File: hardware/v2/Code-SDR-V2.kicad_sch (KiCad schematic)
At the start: 0 parts

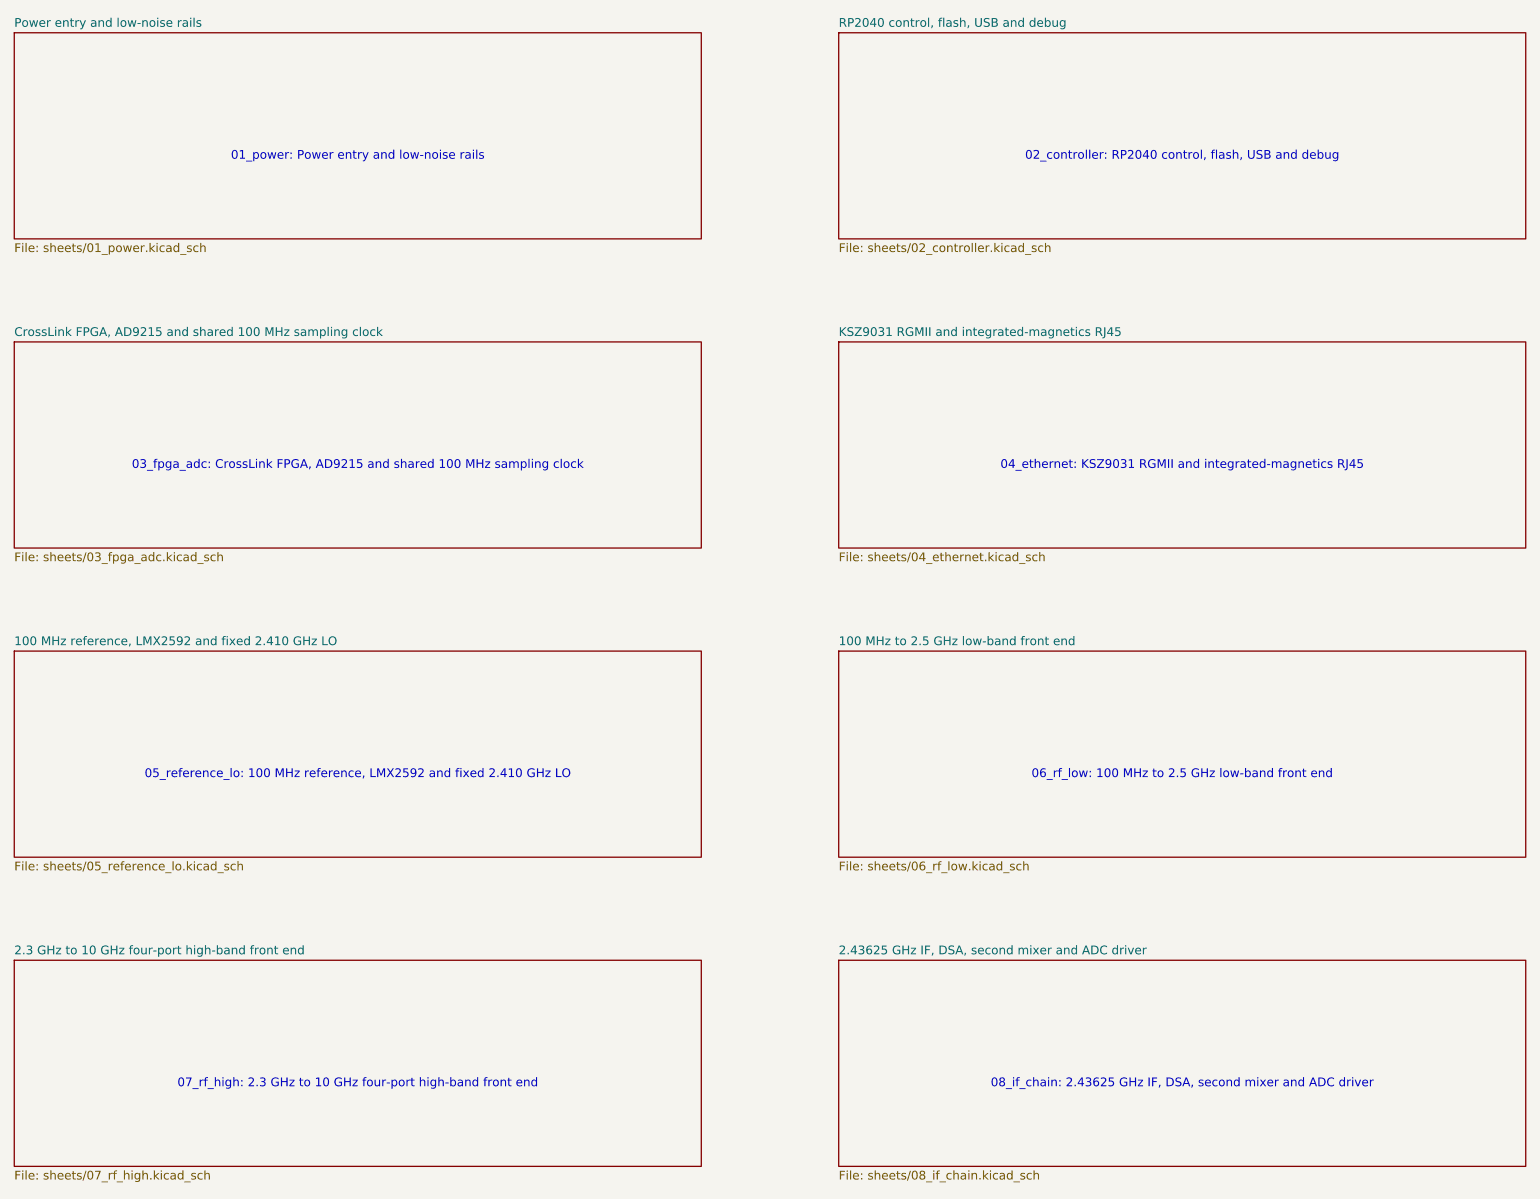
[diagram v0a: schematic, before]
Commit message: hardware: checkpoint corrected V2 routing at 108 opens
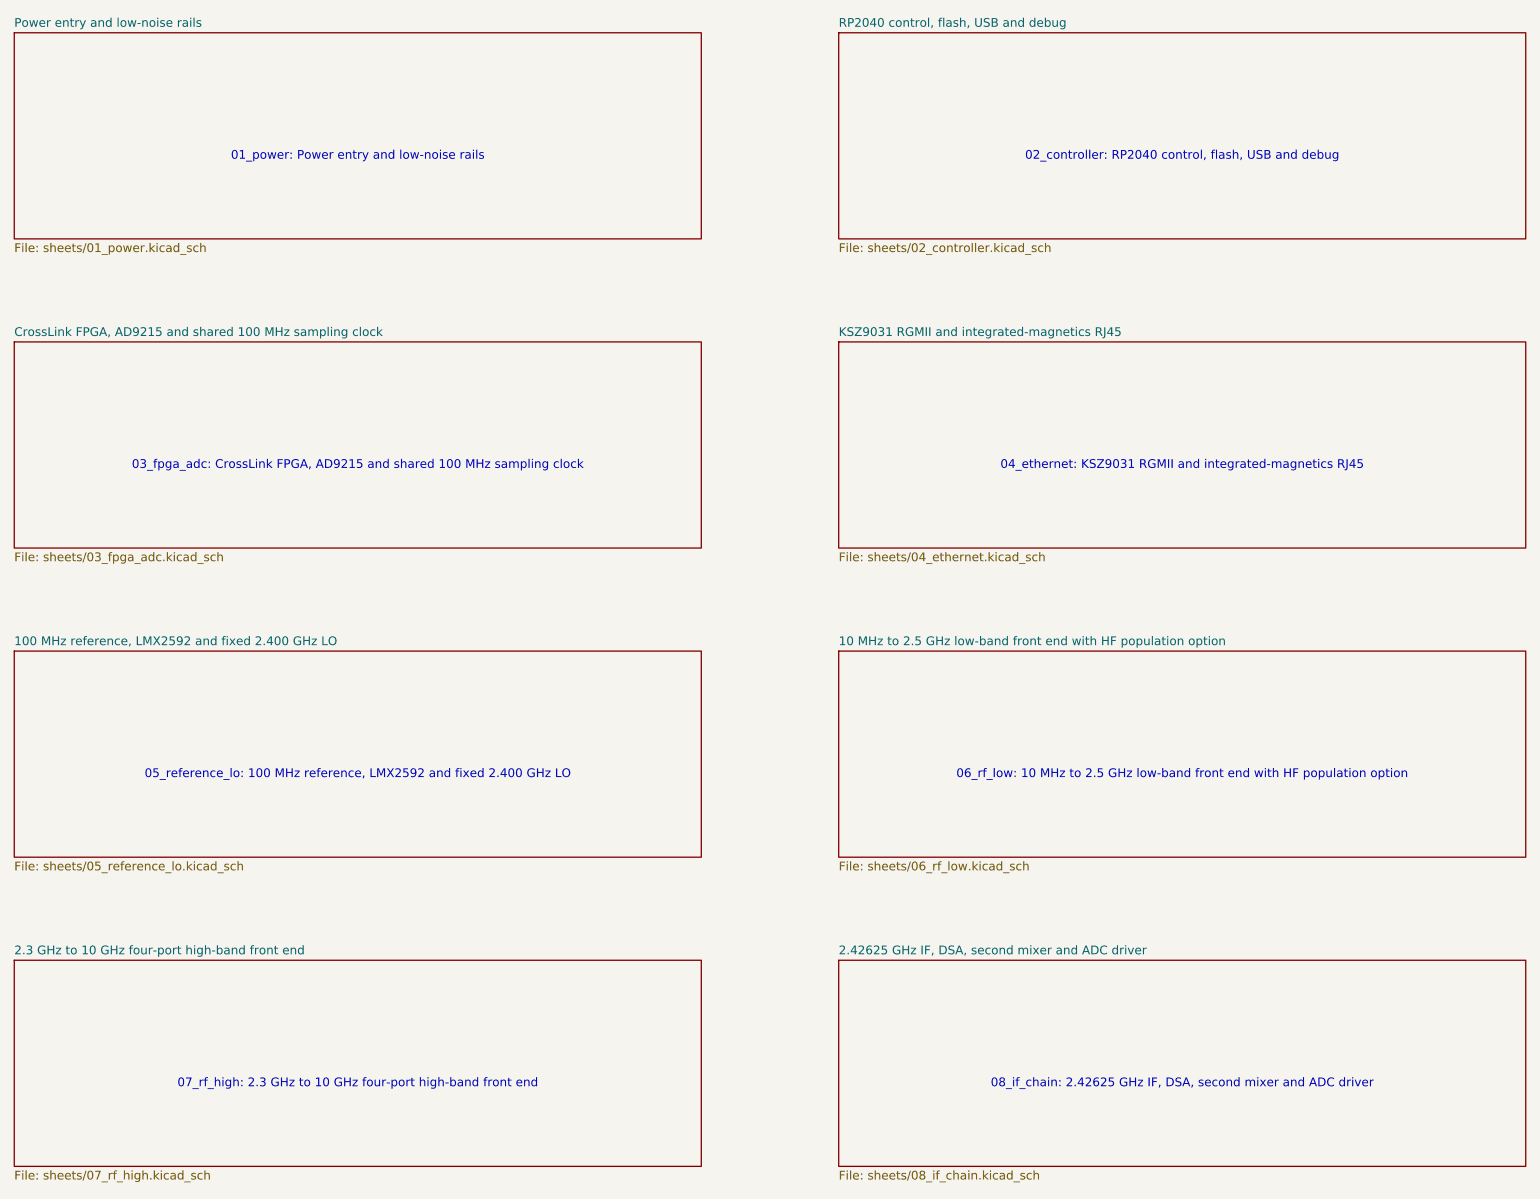
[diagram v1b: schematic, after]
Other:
- sheet 100 MHz reference, LMX2592 and fixed 2.410 GHz LO renamed 100 MHz reference, LMX2592 and fixed 2.400 GHz LO
- sheet 100 MHz to 2.5 GHz low-band front end renamed 10 MHz to 2.5 GHz low-band front end with HF population option
- sheet 2.43625 GHz IF, DSA, second mixer and ADC driver renamed 2.42625 GHz IF, DSA, second mixer and ADC driver
- note added: "05_reference_lo: 100 MHz reference, LMX2592 and fixed 2.400 GHz LO"
- note added: "06_rf_low: 10 MHz to 2.5 GHz low-band front end with HF population option"
- note added: "08_if_chain: 2.42625 GHz IF, DSA, second mixer and ADC driver"
- note removed: "05_reference_lo: 100 MHz reference, LMX2592 and fixed 2.410 GHz LO"
- note removed: "06_rf_low: 100 MHz to 2.5 GHz low-band front end"
- note removed: "08_if_chain: 2.43625 GHz IF, DSA, second mixer and ADC driver"
- title: Code-SDR V2 - 100 MHz to 10 GHz Cost-First Receiver -> Code-SDR V2 - 10 MHz to 10 GHz Receiver with HF Population Option
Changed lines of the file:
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@@
 	(paper "A3")
 	(title_block
-		(title "Code-SDR V2 - 100 MHz to 10 GHz Cost-First Receiver")
+		(title "Code-SDR V2 - 10 MHz to 10 GHz Receiver with HF Population Option")
 		(rev "2.0")
 		(company "Code-SDR")
@@
 		)
 	)
-	(text "05_reference_lo: 100 MHz reference, LMX2592 and fixed 2.410 GHz LO"
+	(text "05_reference_lo: 100 MHz reference, LMX2592 and fixed 2.400 GHz LO"
 		(exclude_from_sim no)
 		(at 75 133 0.0000)
@@
 		)
 	)
-	(text "06_rf_low: 100 MHz to 2.5 GHz low-band front end"
+	(text "06_rf_low: 10 MHz to 2.5 GHz low-band front end with HF population option"
 		(exclude_from_sim no)
 		(at 195 133 0.0000)
@@
 		)
 	)
-	(text "08_if_chain: 2.43625 GHz IF, DSA, second mixer and ADC driver"
+	(text "08_if_chain: 2.42625 GHz IF, DSA, second mixer and ADC driver"
 		(exclude_from_sim no)
 		(at 195 178 0.0000)
@@
 			(color 0 0 0 0.0000)
 		)
-		(property "Sheetname" "100 MHz reference, LMX2592 and fixed 2.410 GHz LO"
+		(property "Sheetname" "100 MHz reference, LMX2592 and fixed 2.400 GHz LO"
 			(at 25 114.2884 0)
 			(effects
@@
 			(color 0 0 0 0.0000)
 		)
-		(property "Sheetname" "100 MHz to 2.5 GHz low-band front end"
+		(property "Sheetname" "10 MHz to 2.5 GHz low-band front end with HF population option"
 			(at 145 114.2884 0)
 			(effects
@@
 			(color 0 0 0 0.0000)
 		)
-		(property "Sheetname" "2.43625 GHz IF, DSA, second mixer and ADC driver"
+		(property "Sheetname" "2.42625 GHz IF, DSA, second mixer and ADC driver"
 			(at 145 159.2884 0)
 			(effects
